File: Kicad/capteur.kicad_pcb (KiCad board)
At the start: 2 copper layers, 68.6 x 54.4 mm, 27 parts, among them J1 Power, J2 Digital/PWM, J3 Analog, J4 Digital/PWM, U2 LTC1050ACN8, U3 MCP41100

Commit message: Small changes of kicad
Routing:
- net Net-(U2-OUT): track 47.1 -> 57.8 mm
- net +5V: track 146.0 -> 154.5 mm
- net /A1: track 11.2 -> 17.6 mm
- net /*6: track 21.7 -> 25.1 mm
- net /R2: track 53.7 -> 55.8 mm
- net /4: track 16.5 -> 17.6 mm
- net /7: track 13.3 -> 14.0 mm
- net /8: track 11.8 -> 12.4 mm

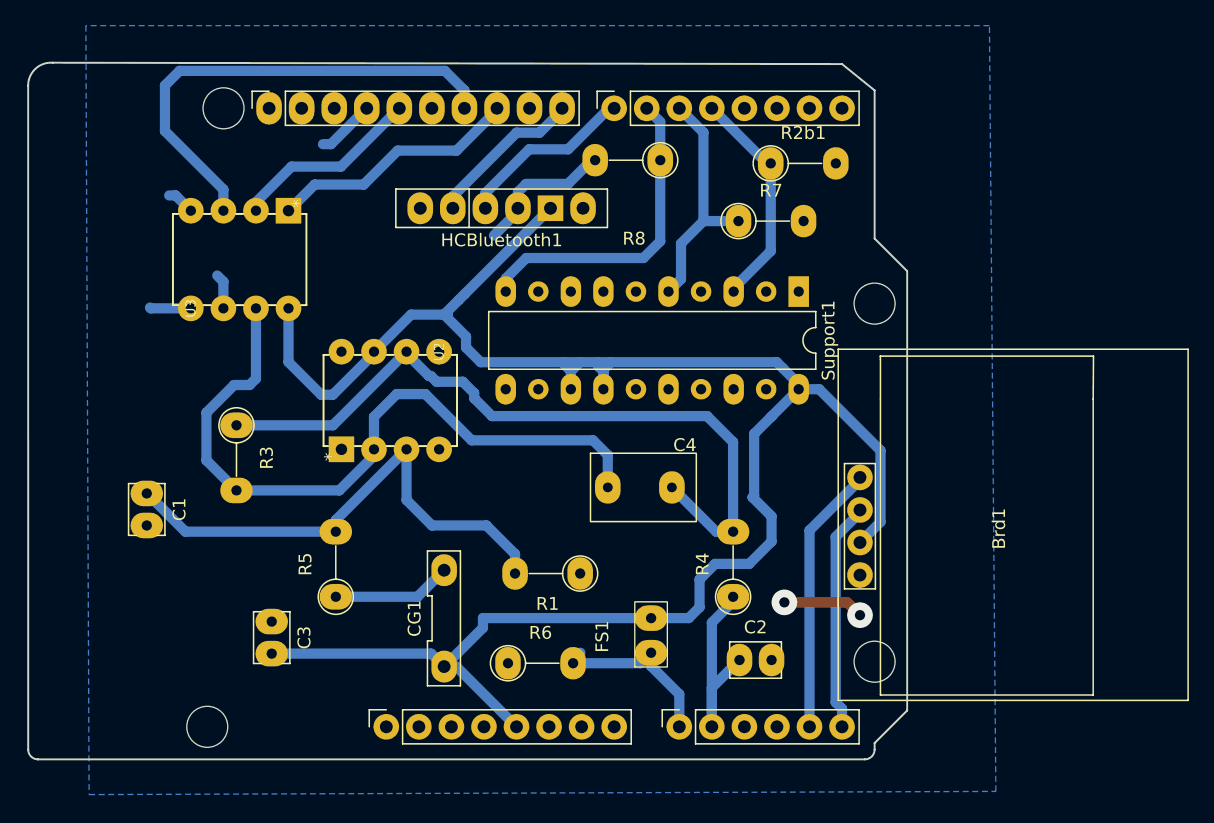
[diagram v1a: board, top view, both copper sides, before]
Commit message: Add of comments and calculation of graphite sensor resistance
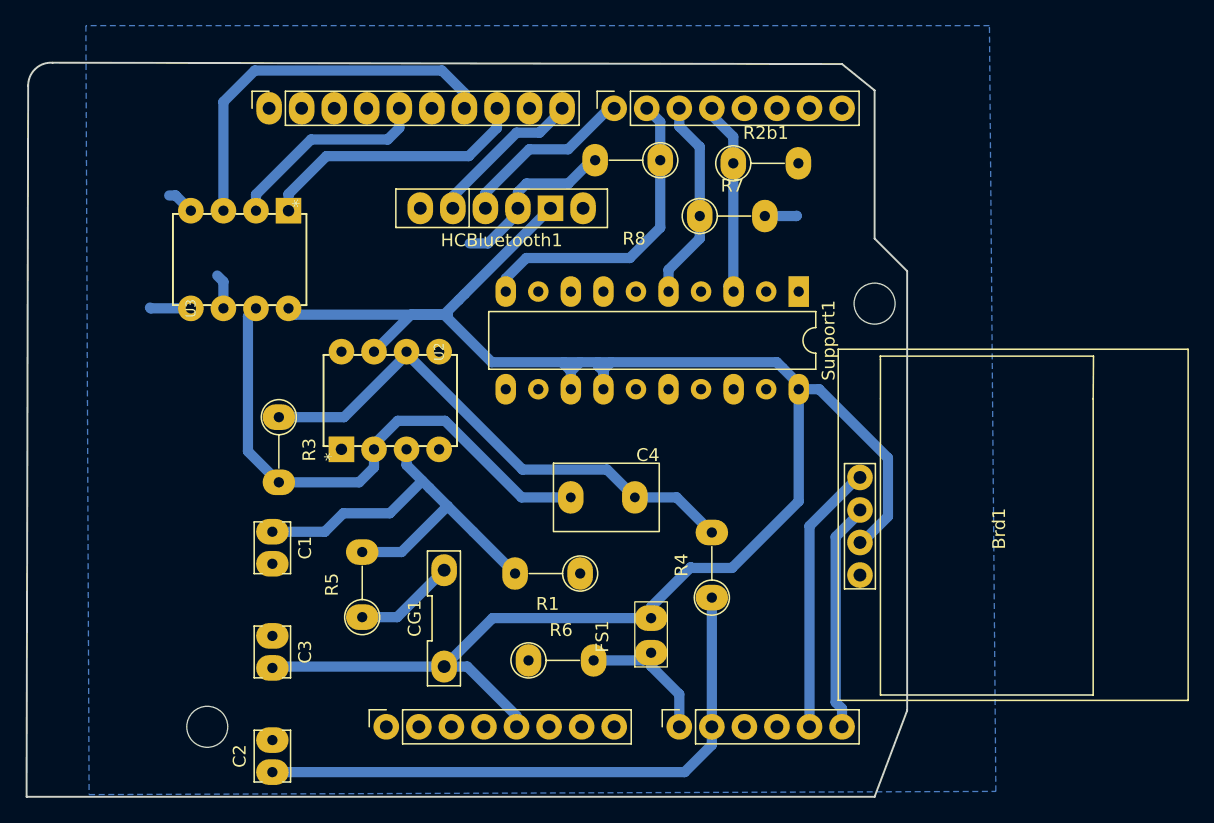
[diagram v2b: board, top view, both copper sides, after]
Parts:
- removed MH1, MH4: MountingHole_3.2mm, Arduino_MountingHole:MountingHole_3.2mm
- moved C2 37.5 mm to (119.0, 101.0), turned to 90 degrees
- moved C1 10.2 mm to (119.0, 82.2)
- moved R3 3.37 mm to (119.6, 73.3)
- moved R7 3.05 mm to (152.4, 57.6)
- moved C4 2.99 mm to (144.8, 77.0)
- moved R2b1 2.92 mm to (155.0, 53.5)
- moved R5 2.60 mm to (126.1, 88.9)
- moved R4 1.66 mm to (153.3, 87.4)
- moved R6 1.62 mm to (139.0, 92.3)
- moved C3 1.12 mm to (119.0, 90.4)
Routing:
- net /A1: track 17.6 -> 46.7 mm
- net Net-(U2-OUT): track 57.8 -> 41.8 mm
- net /R2: track 55.8 -> 43.1 mm
- net /*11: track 38.1 -> 30.8 mm
- net GND: track 30.9 -> 24.7 mm, vias 2 -> 0
- net Net-(U2-+IN): track 40.4 -> 34.7 mm
- net +5V: track 154.5 -> 150.4 mm
- net /*5: track 18.9 -> 16.0 mm
- net /A0: track 13.2 -> 11.4 mm
- net /4: track 17.6 -> 15.9 mm
- net Net-(CG1-Vout): track 9.31 -> 7.91 mm
- net /*10: track 19.9 -> 21.2 mm
- net /13: track 14.9 -> 16.1 mm
- net /*6: track 25.1 -> 24.5 mm
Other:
- board size 68.6 x 54.4 mm -> 68.7 x 57.3 mm
